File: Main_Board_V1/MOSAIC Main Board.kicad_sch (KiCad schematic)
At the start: 77 parts, among them J1 CONN E, J10 QWIIC_RIGHT_ANGLE, J11 Vertical Qwiic Connector, J12 CONN E, J13 CONN E, J14 35RAPC4BH3 CONN 3.5MM, J2 CONN E, J3 CONN E, J4 CONN HEADER VERT 10POS 1.27MM, J5 USB TYPE C R/A SMT 16PIN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

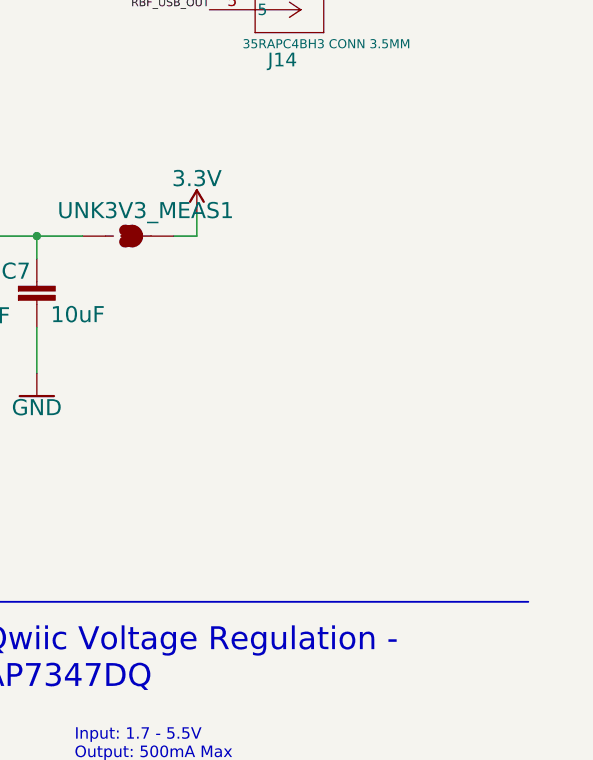
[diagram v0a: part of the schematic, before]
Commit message: Added new board cutout and m3 mount holes
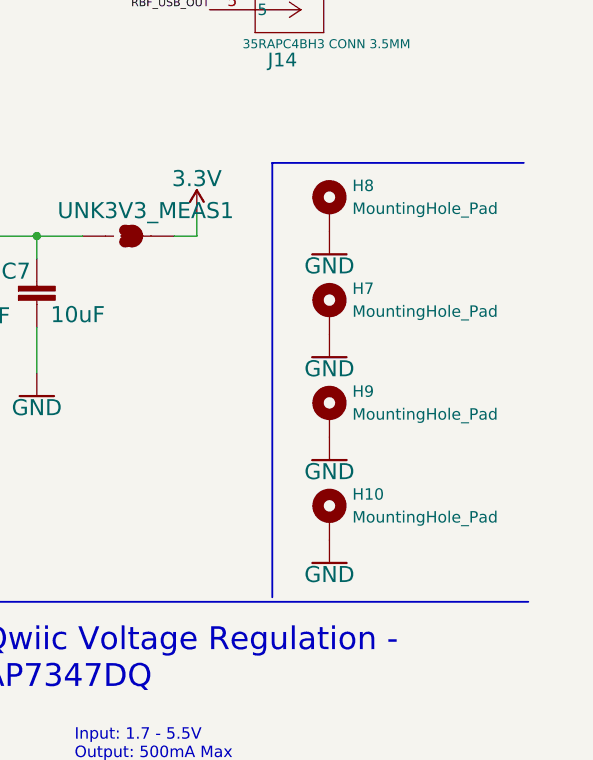
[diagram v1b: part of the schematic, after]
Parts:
- added H10, H9: MountingHole_Pad, main_board_footprints_V1.0:MountingHole_3.2mm_Pad_Oval, symbol Mechanical:MountingHole_Pad
- added H7, H8: MountingHole_Pad, MountingHole:MountingHole_3.2mm_M3_Pad, symbol Mechanical:MountingHole_Pad
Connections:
- net GND: now also H10.1, H7.1, H8.1, H9.1

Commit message: Updated component sourcing
For C2 and C3
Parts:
- C2: Source https://www.digikey.com/en/products/detail/samsung-electro-mechanics/CL21A106KOQNNNE/3886754 -> https://www.digikey.com/en/products/detail/samsung-electro-mechanics/CL21A106KOCLRNC/3888057
- C3: Source (none) -> https://www.mouser.com/ProductDetail/KYOCERA-AVX/KAM21BR71H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
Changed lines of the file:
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@@
 			)
 		)
-		(property "Source" "https://www.digikey.com/en/products/detail/samsung-electro-mechanics/CL21A106KOQNNNE/3886754"
+		(property "Source" "https://www.digikey.com/en/products/detail/samsung-electro-mechanics/CL21A106KOCLRNC/3888057"
 			(at 344.678 69.088 0)
 			(effects
@@
 			)
 		)
+		(property "Source" "https://www.mouser.com/ProductDetail/KYOCERA-AVX/KAM21BR71H104JT?qs=Jm2GQyTW%2Fbic6Zk4McEt6w%3D%3D"
+			(at 352.298 69.088 0)
+			(effects
+				(font
+					(size 1.27 1.27)
+				)
+				(hide yes)
+			)
+		)

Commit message: Updated source for R2
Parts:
- R2: Source https://www.digikey.com/en/products/detail/yageo/RC0603JR-0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 -> https://www.digikey.com/en/products/detail/bourns-inc/CR060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
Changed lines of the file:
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@@
 			)
 		)
-		(property "Source" "https://www.digikey.com/en/products/detail/yageo/RC0603JR-0710KL/726700"
+		(property "Source" "https://www.digikey.com/en/products/detail/bourns-inc/CR0603-FX-1002ELF/3593188"
 			(at 29.718 89.408 0)
 			(effects

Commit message: Updated source for R12
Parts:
- R12: Source https://www.digikey.com/en/products/detail/panasonic-electr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 -> https://www.digikey.com/en/products/detail/bourns-inc/CR060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
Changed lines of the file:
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@@
 			)
 		)
-		(property "Source" "https://www.digikey.com/en/products/detail/panasonic-electronic-components/ERJ-3EKF2001V/196183"
+		(property "Source" "https://www.digikey.com/en/products/detail/bourns-inc/CR0603-FX-2001ELF/3740910"
 			(at 349.758 132.588 0)
 			(effects

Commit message: Updated source for J9
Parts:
- J9: Source https://www.sparkfun.com/products/11641 -> https://www.mouser.com/ProductDetail/Adafruit/1769?qs=GURaw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
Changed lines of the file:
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@@
 			)
 		)
-		(property "Source" "https://www.sparkfun.com/products/11641"
+		(property "Source" "https://www.mouser.com/ProductDetail/Adafruit/1769?qs=GURawfaeGuBbgoGtf2XstA%3D%3D"
 			(at 375.285 134.62 90)
 			(effects

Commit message: Updated source J14
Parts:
- J14: Source https://www.digikey.com/en/products/detail/switchcraft-inc/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 -> https://www.mouser.com/ProductDetail/Switchcraft/35RAPC4BH3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
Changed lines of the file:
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@@
 			)
 		)
-		(property "Source" "https://www.digikey.com/en/products/detail/switchcraft-inc/35RAPC4BH3/1288781"
+		(property "Source" "https://www.mouser.com/ProductDetail/Switchcraft/35RAPC4BH3?qs=I3kMT7EEIOWFGyk5rynRAQ%3D%3D"
 			(at 422.275 26.162 0)
 			(effects

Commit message: Updated source for U2
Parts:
- U2: Source https://www.digikey.com/en/products/detail/diodes-incorpora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 -> https://www.mouser.com/ProductDetail/Diodes-Incorporated/D5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
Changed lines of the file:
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@@
 			)
 		)
-		(property "Source" "https://www.digikey.com/en/products/detail/diodes-incorporated/D5V0P4URL6SO-7/6052566"
+		(property "Source" "https://www.mouser.com/ProductDetail/Diodes-Incorporated/D5V0P4URL6SO-7?qs=rN85NNvew%2FTFk6tlkCQ5yQ%3D%3D"
 			(at 278.638 69.088 0)
 			(effects

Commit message: Updated footprint for S1
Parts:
- S1: footprint SparkFun_Main_Board_Double_v22:SWITCH_SPST_SMD_A -> main_board_footprints_V1.0:SWITCH_SPST_SMD_A
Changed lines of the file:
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@@
 			)
 		)
-		(property "Footprint" "SparkFun_Main_Board_Double_v22:SWITCH_SPST_SMD_A"
+		(property "Footprint" "main_board_footprints_V1.0:SWITCH_SPST_SMD_A"
 			(at 169.418 107.188 0)
 			(effects
